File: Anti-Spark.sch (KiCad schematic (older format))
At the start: 19 parts, among them IC1 BQ76200PWR, IC2 TPS7A4101DGNR, J1 Conn_01x04_Male, Q1 IRFS7530TRL7PP, Q2 IRFS7530TRL7PP

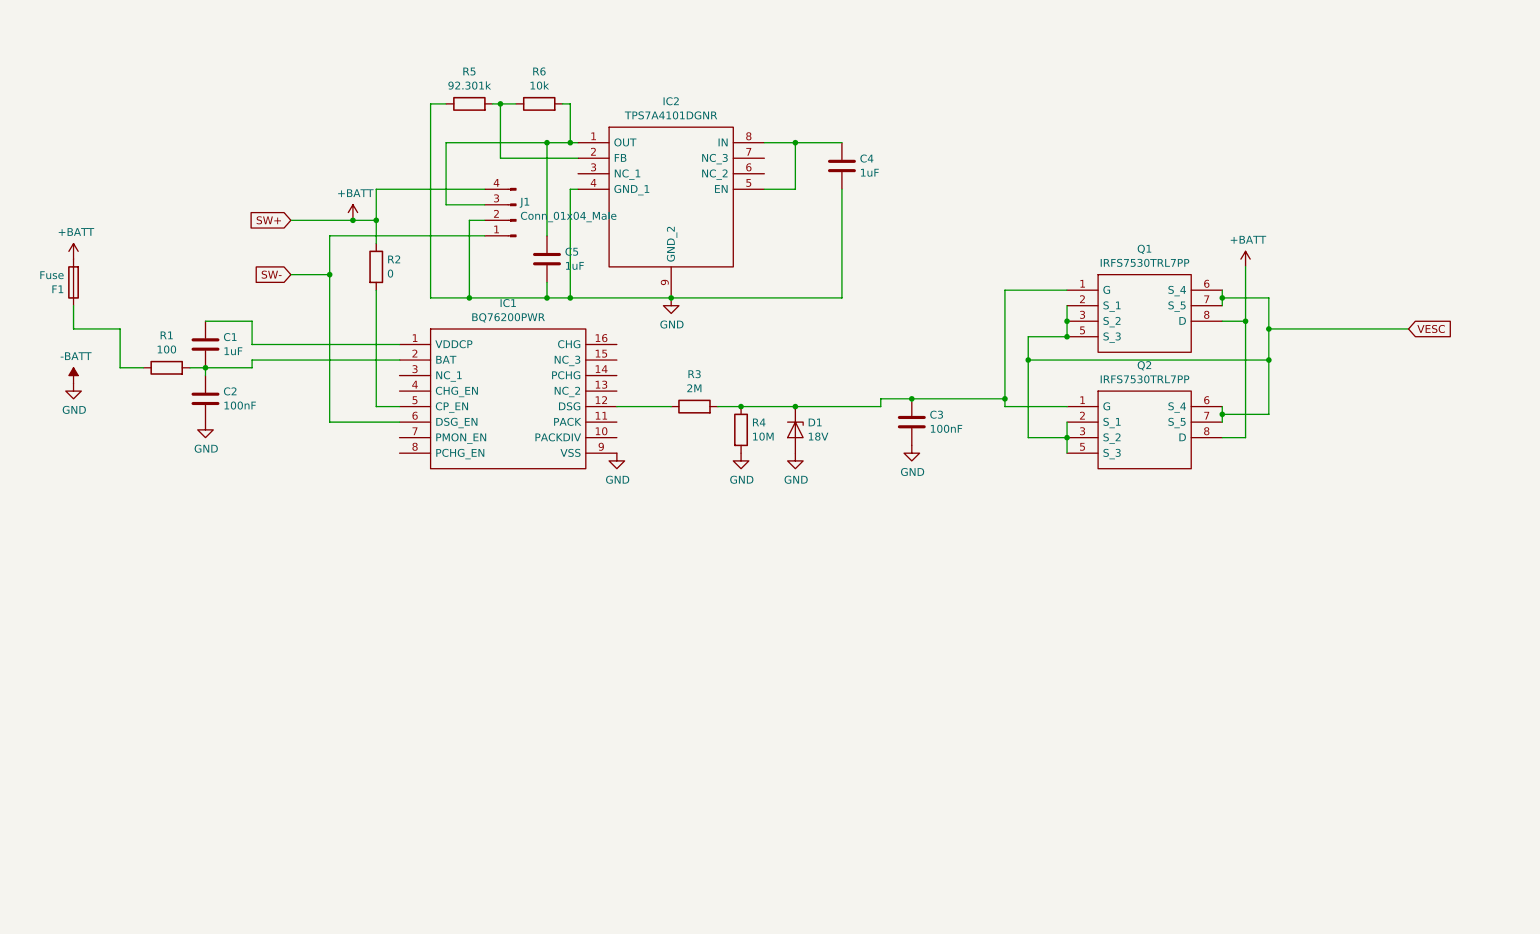
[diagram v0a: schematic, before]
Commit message: ch: new version with 10 mosfets
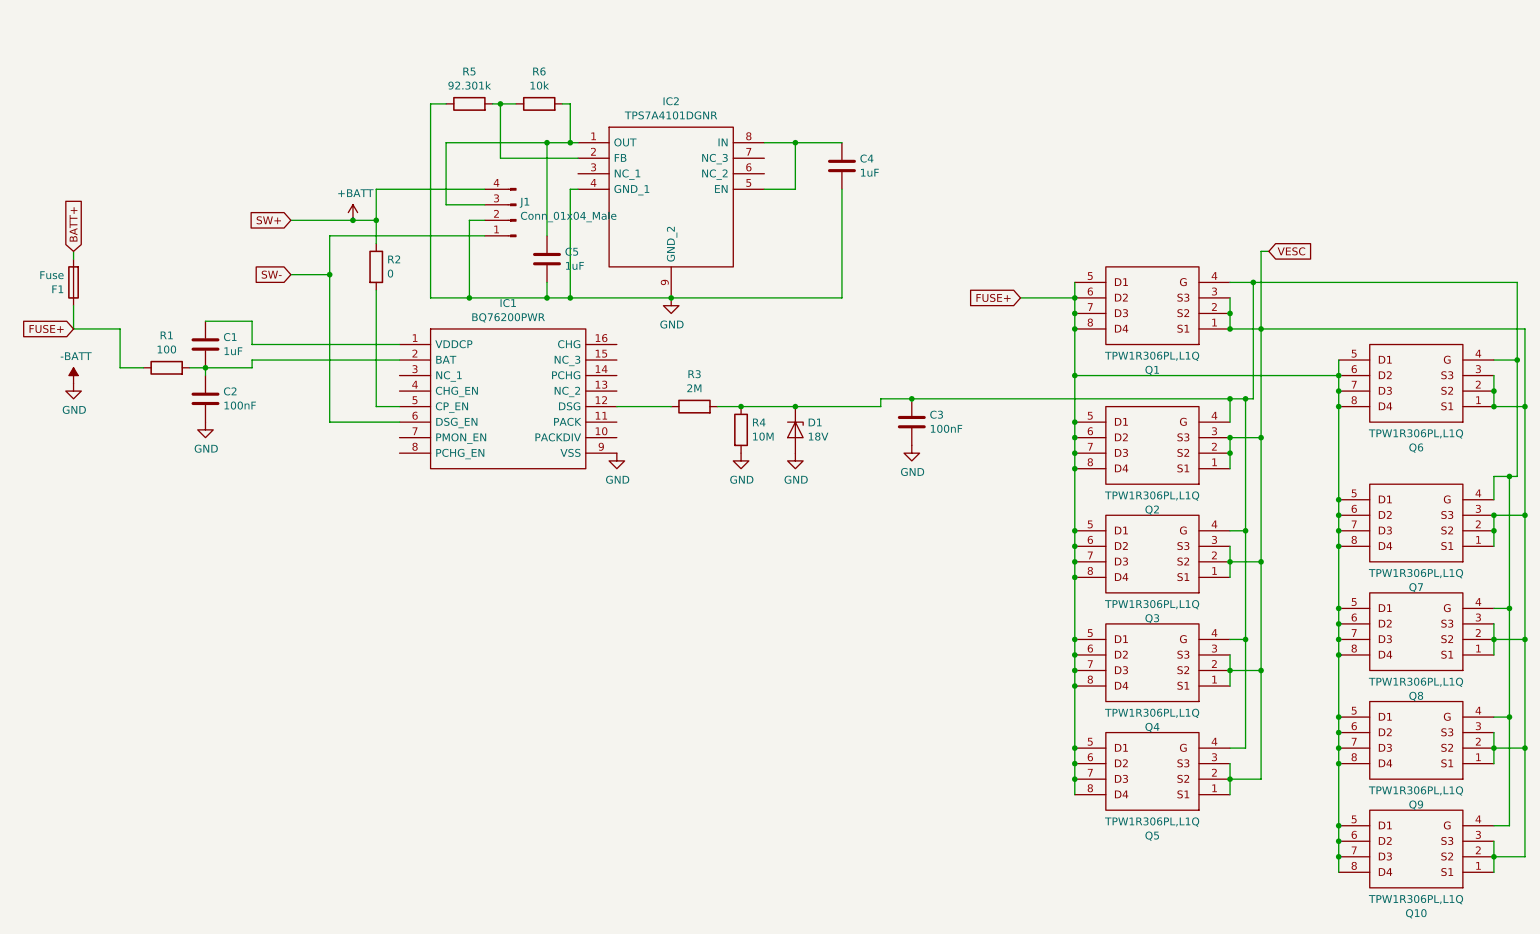
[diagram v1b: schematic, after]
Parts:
- removed +BATT: +BATT, symbol power:+BATT
- removed Q1, Q2: IRFS7530TRL7PP, SamacSys_Parts:IRFS7530, symbol SamacSys_Parts:IRFS7530TRL7PP
- added Q1, Q10, Q2, Q3, Q4, Q5, Q6, Q7, Q8, Q9: TPW1R306PL,L1Q, SOP_ADVANCE, symbol SamacSys_Parts:TPW1R306PL,L1Q
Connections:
- net +BATT: no longer F1.2
- net VESC: now also Q1.1, Q1.2, Q1.3, Q10.1, Q10.2, Q10.3, Q2.1, Q2.2, Q2.3, Q3.1, Q3.2, Q3.3, Q4.1, Q4.2, Q4.3, Q5.1, Q5.2, Q5.3, Q6.1, Q6.2, Q6.3, Q7.1, Q7.2, Q7.3, Q8.1, Q8.2, Q8.3, Q9.1, Q9.2, Q9.3
- net at C3.1, D1.1 (K), R3.2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: now also Q1.4, Q10.4, Q2.4, Q3.4, Q4.4, Q5.4, Q6.4, Q7.4, Q8.4, Q9.4
- net FUSE+: now reaches F1.1, R1.1
- net FUSE+: now also Q1.5, Q1.6, Q1.7, Q1.8, Q10.5, Q10.6, Q10.7, Q10.8, Q2.5, Q2.6, Q2.7, Q2.8, Q3.5, Q3.6, Q3.7, Q3.8, Q4.5, Q4.6, Q4.7, Q4.8, Q5.5, Q5.6, Q5.7, Q5.8, Q6.5, Q6.6, Q6.7, Q6.8, Q7.5, Q7.6, Q7.7, Q7.8, Q8.5, Q8.6, Q8.7, Q8.8, Q9.5, Q9.6, Q9.7, Q9.8
- new net BATT+: F1.2

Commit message: updated schematic to V0.2 Board file is corrupted
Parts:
- added C6: 1uF, Capacitor_SMD:C_0805_2012Metric_Pad1.15x1.40mm_HandSolder, symbol Device:C
- added R7, R8: 1M, Resistor_SMD:R_0805_2012Metric_Pad1.15x1.40mm_HandSolder, symbol Device:R
- D1: value 18V -> 10V
- R2: value 0 -> 1k
- R3: value 2M -> 1M
- R5: value 92.301k -> 500k
- R6: value 10k -> 50k
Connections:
- net labels added: +12V
- net labels removed: +BATT, SW+
- wire segments 168 -> 176
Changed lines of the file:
@@
 	1800 2650 1650 2650
 Wire Wire Line
-	1650 2650 1650 2400
-Wire Wire Line
 	2500 2500 3450 2500
 Wire Wire Line
 	2500 2600 3450 2600
-Wire Wire Line
-	3300 2150 3300 2900
-Wire Wire Line
-	3300 2900 3450 2900
-Wire Wire Line
-	3000 3000 3450 3000
 $Comp
 L Device:R R1
@@
 	0    -1   -1   0
 $EndComp
-$Comp
-L Device:R R2
-U 1 1 5D71E123
-P 3300 2000
-F 0 "R2" H 3370 2046 50  0000 L CNN
-F 1 "0" H 3370 1955 50  0000 L CNN
-F 2 "Resistor_SMD:R_0805_2012Metric_Pad1.15x1.40mm_HandSolder" V 3230 2000 50  0001 C CNN
-F 3 "~" H 3300 2000 50  0001 C CNN
-	1    3300 2000
-	1    0    0    -1
-$EndComp
-Wire Wire Line
-	3300 1850 3300 1700
-Wire Wire Line
-	3300 1700 3150 1700
-$Comp
-L power:+BATT #PWR05
-U 1 1 5D725D55
-P 3150 1700
-F 0 "#PWR05" H 3150 1550 50  0001 C CNN
-F 1 "+BATT" H 3165 1873 50  0000 C CNN
-F 2 "" H 3150 1700 50  0001 C CNN
-F 3 "" H 3150 1700 50  0001 C CNN
-	1    3150 1700
-	1    0    0    -1
-$EndComp
-Text GLabel 2750 1700 0    50   Input ~ 0
-SW+
 Text GLabel 2750 2050 0    50   Input ~ 0
 SW-
 Wire Wire Line
-	2750 1700 3150 1700
-Connection ~ 3150 1700
-Wire Wire Line
 	2750 2050 3000 2050
-Wire Wire Line
-	3000 2050 3000 3000
 $Comp
 L Device:R R3
@@
 P 5350 2900
 F 0 "R3" V 5557 2900 50  0000 C CNN
-F 1 "2M" V 5466 2900 50  0000 C CNN
+F 1 "1M" V 5466 2900 50  0000 C CNN
 F 2 "Resistor_SMD:R_0805_2012Metric_Pad1.15x1.40mm_HandSolder" V 5280 2900 50  0001 C CNN
 F 3 "~" H 5350 2900 50  0001 C CNN
@@
 P 6000 3050
 F 0 "D1" V 5954 3129 50  0000 L CNN
-F 1 "18V" V 6045 3129 50  0000 L CNN
+F 1 "10V" V 6045 3129 50  0000 L CNN
 F 2 "Diode_SMD:D_SOD-323_HandSoldering" H 6000 3050 50  0001 C CNN
 F 3 "~" H 6000 3050 50  0001 C CNN
 	1    6000 3050
 	0    1    1    0
-$EndComp
-$Comp
-L power:GND #PWR08
-U 1 1 5D73EDC3
-P 6000 3200
-F 0 "#PWR08" H 6000 2950 50  0001 C CNN
-F 1 "GND" H 6005 3027 50  0000 C CNN
-F 2 "" H 6000 3200 50  0001 C CNN
-F 3 "" H 6000 3200 50  0001 C CNN
-	1    6000 3200
-	1    0    0    -1
 $EndComp
 Wire Wire Line
@@
 $EndComp
 $Comp
-L power:GND #PWR07
-U 1 1 5D72FE62
-P 5650 3200
-F 0 "#PWR07" H 5650 2950 50  0001 C CNN
-F 1 "GND" H 5655 3027 50  0000 C CNN
-F 2 "" H 5650 3200 50  0001 C CNN
-F 3 "" H 5650 3200 50  0001 C CNN
-	1    5650 3200
-	1    0    0    -1
-$EndComp
-$Comp
-L power:GND #PWR09
-U 1 1 5D732663
-P 6750 3150
-F 0 "#PWR09" H 6750 2900 50  0001 C CNN
-F 1 "GND" H 6755 2977 50  0000 C CNN
-F 2 "" H 6750 3150 50  0001 C CNN
-F 3 "" H 6750 3150 50  0001 C CNN
-	1    6750 3150
-	1    0    0    -1
-$EndComp
-$Comp
 L Device:C C3
 U 1 1 5D73080B
@@
 Wire Wire Line
 	6550 2850 6750 2850
-$Comp
-L Device:Fuse F1
-U 1 1 5D75F413
-P 1350 2100
-F 0 "F1" H 1410 2146 50  0000 L CNN
-F 1 "Fuse" H 1410 2055 50  0000 L CNN
-F 2 "SamacSys_Parts:littleFuseBF1" V 1280 2100 50  0001 C CNN
-F 3 "~" H 1350 2100 50  0001 C CNN
-	1    1350 2100
-	-1   0    0    1
-$EndComp
-Wire Wire Line
-	1350 2400 1650 2400
-Wire Wire Line
-	3300 1500 3300 1700
-Connection ~ 3300 1700
 Wire Wire Line
 	3000 1800 3000 2050
-Connection ~ 3000 2050
 $Comp
 L SamacSys_Parts:TPS7A4101DGNR IC2
@@
 	6300 2200 5200 2200
 $Comp
-L Device:R R6
-U 1 1 5D76B68B
-P 4350 950
-F 0 "R6" V 4557 950 50  0000 C CNN
-F 1 "10k" V 4466 950 50  0000 C CNN
-F 2 "Resistor_SMD:R_0805_2012Metric_Pad1.15x1.40mm_HandSolder" V 4280 950 50  0001 C CNN
-F 3 "~" H 4350 950 50  0001 C CNN
-	1    4350 950
-	0    -1   -1   0
-$EndComp
-$Comp
 L Device:R R5
 U 1 1 5D76D111
 P 3900 950
 F 0 "R5" V 4107 950 50  0000 C CNN
-F 1 "92.301k" V 4016 950 50  0000 C CNN
+F 1 "500k" V 4016 950 50  0000 C CNN
 F 2 "Resistor_SMD:R_0805_2012Metric_Pad1.15x1.40mm_HandSolder" V 3830 950 50  0001 C CNN
 F 3 "~" H 3900 950 50  0001 C CNN
@@
 $EndComp
 Wire Wire Line
-	4550 1200 4550 950
+	4550 1200 4550 1150
 Wire Wire Line
 	4550 950  4500 950
@@
 Connection ~ 3900 2200
 Wire Wire Line
-	4100 950  4100 1300
+	4100 950  4100 1150
 Wire Wire Line
 	4100 1300 4600 1300
@@
 	8900 5100 8900 4400
 Connection ~ 8900 4400
-Text GLabel 1350 1900 1    50   Input ~ 0
-BATT+
 Wire Wire Line
 	1350 1900 1350 1950
@@
 	-1   0    0    1
 $EndComp
+$Comp
+L Device:R R6
+U 1 1 5D76B68B
+P 4350 950
+F 0 "R6" V 4557 950 50  0000 C CNN
+F 1 "50k" V 4466 950 50  0000 C CNN
+F 2 "Resistor_SMD:R_0805_2012Metric_Pad1.15x1.40mm_HandSolder" V 4280 950 50  0001 C CNN
+F 3 "~" H 4350 950 50  0001 C CNN
+	1    4350 950
+	0    -1   -1   0
+$EndComp
+$Comp
+L power:+12V #PWR05
+U 1 1 5D9E9B36
+P 4550 950
+F 0 "#PWR05" H 4550 800 50  0001 C CNN
+F 1 "+12V" H 4565 1123 50  0000 C CNN
+F 2 "" H 4550 950 50  0001 C CNN
+F 3 "" H 4550 950 50  0001 C CNN
+	1    4550 950
+	1    0    0    -1
+$EndComp
+Connection ~ 4550 950
+$Comp
+L Device:C C6
+U 1 1 5D9EA02A
+P 4350 1150
+F 0 "C6" H 4465 1196 50  0000 L CNN
+F 1 "1uF" H 4465 1105 50  0000 L CNN
+F 2 "Capacitor_SMD:C_0805_2012Metric_Pad1.15x1.40mm_HandSolder" H 4388 1000 50  0001 C CNN
+F 3 "~" H 4350 1150 50  0001 C CNN
+	1    4350 1150
+	0    -1   -1   0
+$EndComp
+Wire Wire Line
+	4500 1150 4550 1150
+Connection ~ 4550 1150
+Wire Wire Line
+	4550 1150 4550 950
+Wire Wire Line
+	4200 1150 4100 1150
+Connection ~ 4100 1150
+Wire Wire Line
+	4100 1150 4100 1300
+Wire Wire Line
+	6750 3150 6750 3200
+Wire Wire Line
+	6000 3200 5650 3200
+Connection ~ 6000 3200
+Text GLabel 7300 3200 2    50   Input ~ 0
+VESC
+$Comp
+L power:+12V #PWR01
+U 1 1 5DA397DF
+P 3100 2850
+F 0 "#PWR01" H 3100 2700 50  0001 C CNN
+F 1 "+12V" H 3115 3023 50  0000 C CNN
+F 2 "" H 3100 2850 50  0001 C CNN
+F 3 "" H 3100 2850 50  0001 C CNN
+	1    3100 2850
+	1    0    0    -1
+$EndComp
+Wire Wire Line
+	3100 2900 3100 2850
+Wire Wire Line
+	3100 2900 3450 2900
+Wire Wire Line
+	3100 2900 3000 2900
+Wire Wire Line
+	3000 2900 3000 3000
+Connection ~ 3100 2900
+Text GLabel 3300 1500 0    50   Input ~ 0
+FUSE+
+Text GLabel 6800 1200 2    50   Input ~ 0
+SW-
+Wire Wire Line
+	6500 1200 6300 1200
+Connection ~ 6300 1200
+Wire Wire Line
+	1650 2650 1650 2400
+$Comp
+L Device:R R2
+U 1 1 5DA7FB94
+P 6650 1200
+F 0 "R2" V 6857 1200 50  0000 C CNN
+F 1 "1k" V 6766 1200 50  0000 C CNN
+F 2 "Resistor_SMD:R_0805_2012Metric_Pad1.15x1.40mm_HandSolder" V 6580 1200 50  0001 C CNN
+F 3 "~" H 6650 1200 50  0001 C CNN
+	1    6650 1200
+	0    -1   -1   0
+$EndComp
+Wire Wire Line
+	1350 2400 1650 2400
+$Comp
+L Device:R R8
+U 1 1 5DA040BA
+P 6950 3200
+F 0 "R8" V 7157 3200 50  0000 C CNN
+F 1 "1M" V 7066 3200 50  0000 C CNN
+F 2 "Resistor_SMD:R_0805_2012Metric_Pad1.15x1.40mm_HandSolder" V 6880 3200 50  0001 C CNN
+F 3 "~" H 6950 3200 50  0001 C CNN
+	1    6950 3200
+	0    -1   -1   0
+$EndComp
+$Comp
+L Device:R R7
+U 1 1 5DA12599
+P 6400 3350
+F 0 "R7" V 6607 3350 50  0000 C CNN
+F 1 "1M" V 6516 3350 50  0000 C CNN
+F 2 "Resistor_SMD:R_0805_2012Metric_Pad1.15x1.40mm_HandSolder" V 6330 3350 50  0001 C CNN
+F 3 "~" H 6400 3350 50  0001 C CNN
+	1    6400 3350
+	-1   0    0    1
+$EndComp
+$Comp
+L power:GND #PWR0102
+U 1 1 5DA197F5
+P 6400 3500
+F 0 "#PWR0102" H 6400 3250 50  0001 C CNN
+F 1 "GND" H 6405 3327 50  0000 C CNN
+F 2 "" H 6400 3500 50  0001 C CNN
+F 3 "" H 6400 3500 50  0001 C CNN
+	1    6400 3500
+	1    0    0    -1
+$EndComp
+Wire Wire Line
+	7100 3200 7300 3200
+Wire Wire Line
+	6800 3200 6750 3200
+Connection ~ 6750 3200
+Wire Wire Line
+	6000 3200 6400 3200
+Connection ~ 6400 3200
+Wire Wire Line
+	6400 3200 6750 3200
+Wire Wire Line
+	3000 3000 3450 3000
+Text GLabel 1350 1900 1    50   Input ~ 0
+BATT+
+$Comp
+L Device:Fuse F1
+U 1 1 5D75F413
+P 1350 2100
+F 0 "F1" H 1410 2146 50  0000 L CNN
+F 1 "Fuse" H 1410 2055 50  0000 L CNN
+F 2 "SamacSys_Parts:littleFuseBF1" V 1280 2100 50  0001 C CNN
+F 3 "~" H 1350 2100 50  0001 C CNN
+	1    1350 2100
+	-1   0    0    1
+$EndComp
